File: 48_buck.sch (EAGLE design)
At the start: 31 parts

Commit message: Update with values from quickstart sheet
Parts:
- removed R13: 10K, rcl:R-TRIMM3224W
- added C16: 1uF, rcl:C-EUC1206
- added C17: .1uF, rcl:C-EUC0805
- added C18: .01uF, rcl:C-EUC0805
- added D1, D2: (no value), zetex:VAR2SOT23
- added J1, J2: POWERPOLE_POWER45A_HORIZONTAL_DRILL, powerpoles:POWERPOLE_POWER45A_HORIZONTAL_DRILL
- added J3: POWERPOLE_POWER10AWG, powerpoles:POWERPOLE_POWER10AWG
- added Q1, Q2: BUZ21, transistor-fet:BUZ21
- C1: value 220uF -> 61.2uF; device rcl:CPOL-USE10-25 -> rcl:C-EUC0805
- C10, C11, C12, C13: value 100uF -> 330uF; device rcl:C-EUC0805 -> resistor:CPOL-USE5-10.5
- C14: device rcl:C-EUC0805 -> rcl:C-EUC1210
- C15: value 100uF -> 10uF; device rcl:C-EUC0805 -> rcl:C-EUC1206
- C3: value .22uF -> 910pF
- C4: value 560pF -> 33pF
- C5: value (none) -> 0.1uF
- C6: value (none) -> 1100pF
- C7: value 100uF -> 1uF
- C8: value 1uF -> 0.47uF
- C9: value 100uF -> 1uF; device rcl:C-EUC0805 -> rcl:C-EUC1206
- L1: value 15uH -> 10uH; device rcl:L-US0207/15 -> rcl:L-USTJ5-U2
- R1: value 390K -> 75K; device rcl:R-US_R0805 -> rcl:R-US_R1206
- R10: value 1M -> 10K2
- R11: value 315K -> 1K; device rcl:R-US_R0805 -> rcl:R-TRIMM3224W
- R12: value 10K -> 3m 1%
- R2: value 11K -> 500R; device rcl:R-US_R0805 -> rcl:R-TRIMM3224W
- R3: value 12.4K -> 1K8; device rcl:R-US_R0805 -> rcl:R-US_R1206
- R4: value (none) -> 1M
- R5: value 1K -> 300K
- R6: value 1k -> 12.4K
- R7: value 3m -> 71K5
- R8: value 1M -> 634K
- R9: value 300K -> 1K
- renumbered U$1 to LM5116
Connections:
- removed net N$13: R12.1, R13.S, R5.2
- removed net V+: C1.+, LM5116.VIN, R1.2, R8.2
- new net N$16: R10.1, R11.E, R11.S
- new net N$17: C1.1, D2.C, J2.V+, J3.V+, LM5116.VIN, Q1.D, R1.2, R4.2
- new net N$19: C4.2, LM5116.FB, R10.2, R7.2, R9.1
- new net N$20: C8.2, L1.1, LM5116.SW, Q1.S, Q2.D
- net GND: now also C2.2, C5.2, C6.2, R3.1, R9.2; no longer C3.2, C4.2, LM5116.VCCX, R2.2, R3.2
- net N$1: now also R2.S, R3.2; no longer LM5116.UVLO, R1.1, R2.1
- net N$10: now also C8.1, D1.C, LM5116.HB; no longer C8.2, L1.1, LM5116.SW
- net N$11: now also C2.1, D2.A, LM5116.UVLO, R1.1, R2.A; no longer C10.1, C11.1, C12.1, C13.1, C14.1, C15.1, C7.1, C9.1, L1.2, LM5116.VOUT, R13.A, R5.1
- net N$12: now also LM5116.HO, Q1.G; no longer C8.1, LM5116.HB
- net N$14: now also C10.+, C11.+, C12.+, C13.+, C14.1, C15.1, C16.1, C17.1, C18.1, C7.1, J1.V+, L1.2, LM5116.VCCX, LM5116.VOUT, R11.A; no longer JP1.2, LM5116.EN, R10.2
- net N$15: now also Q2.S, R12.1; no longer R7.1
- net N$2: now also LM5116.EN, R4.1, R5.2; no longer R8.1, R9.2
- net N$3: now also C5.1; no longer C3.1
- net N$4: now also C9.1, D1.A, R8.2; no longer C2.1, R11.2
- net N$5: now also C3.2, R7.1; no longer C5.2, R4.1
- net N$6: now also R6.1; no longer R3.1
- net N$7: now also C3.1, C4.1; no longer C5.1, C6.1
- net N$8: now also LM5116.LO, Q2.G; no longer C6.2, LM5116.FB, R12.2, R4.2, R6.1
- net N$9: now also C6.1, R8.1; no longer C4.1, R11.1
- net PE: now also C1.2, C10.-, C11.-, C12.-, C13.-, C16.2, C17.2, C18.2, J1.GND, J2.GND, J3.GND, JP1.2, R12.2, R5.1; no longer C1.-, C10.2, C11.2, C12.2, C13.2, C2.2, R10.1, R7.2, R9.1
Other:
- note added: "LM5116"
- moved on the sheet: C14, C15, C2, C3, C4, C5, C6, C7, C8, C9, JP1, L1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

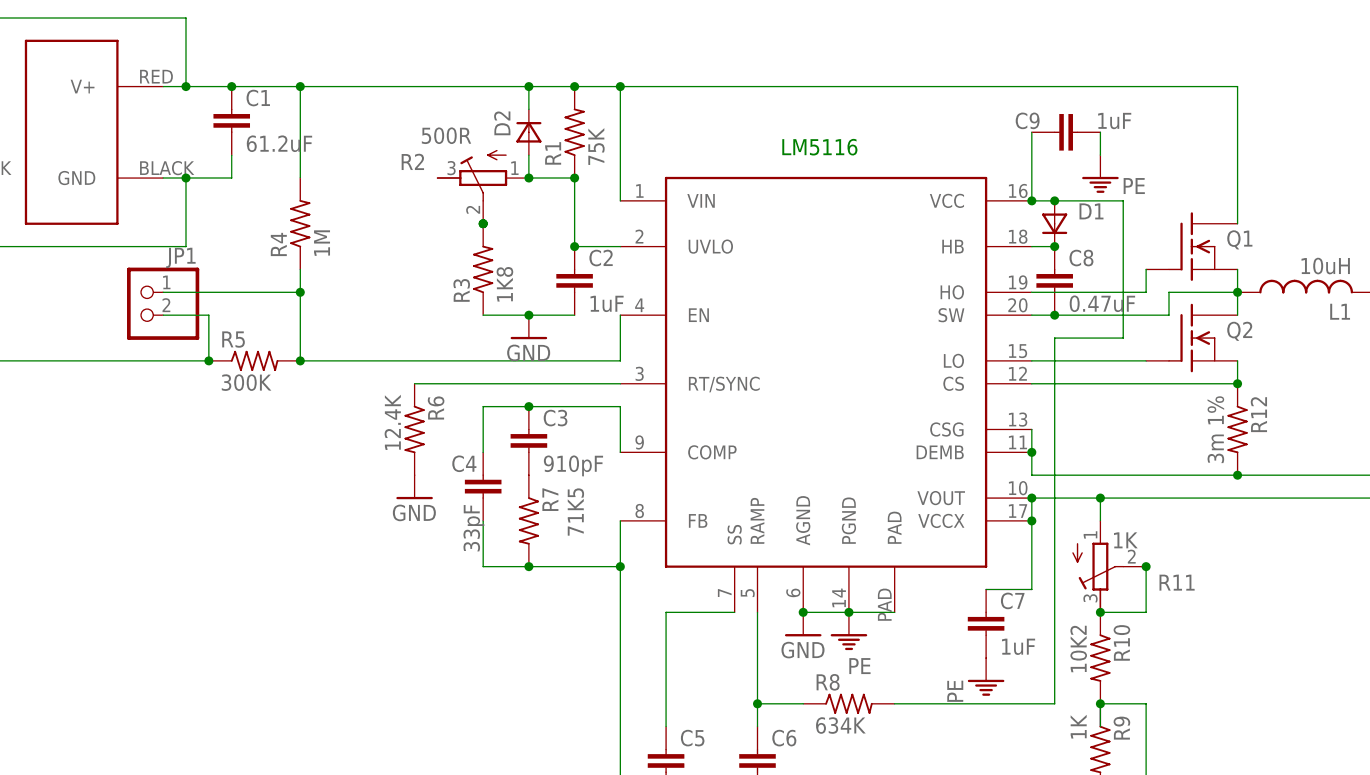
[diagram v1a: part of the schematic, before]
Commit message: Verified schematic, added components to library, started layout
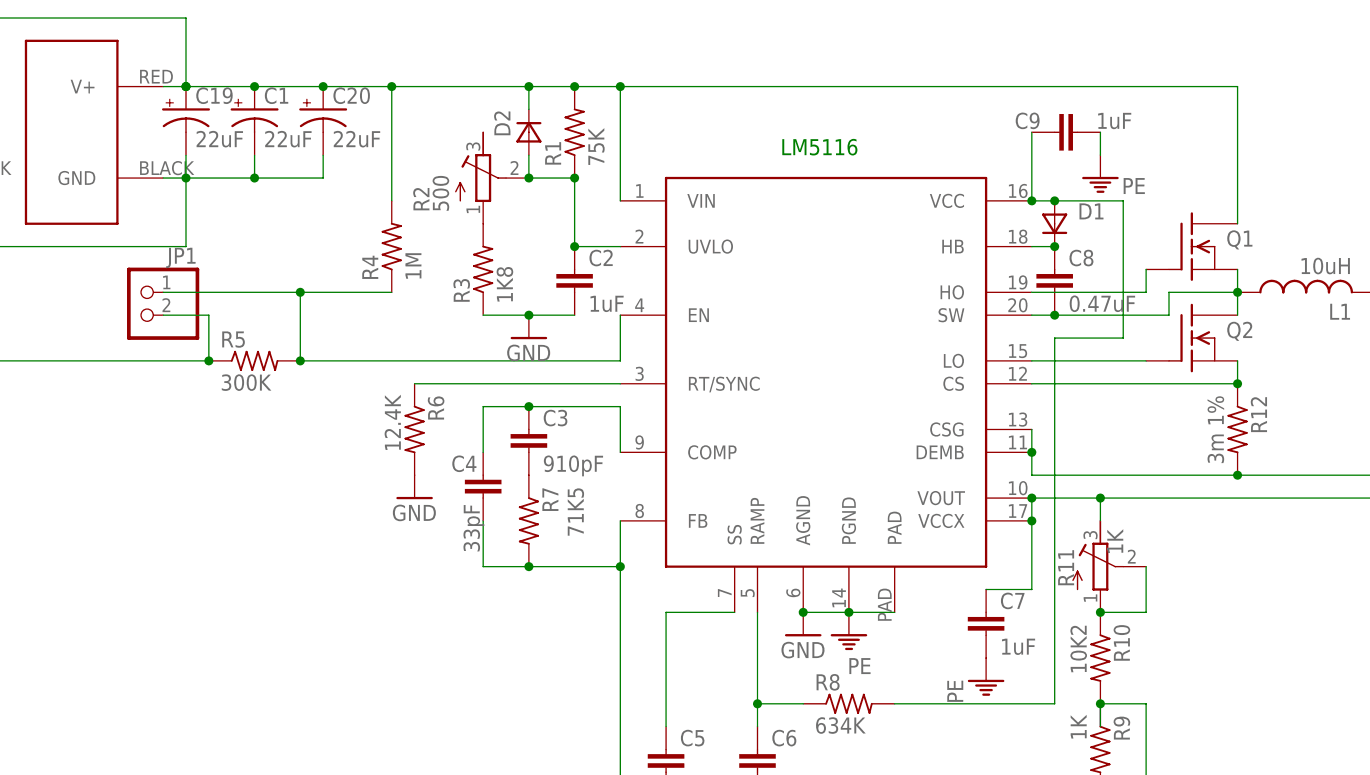
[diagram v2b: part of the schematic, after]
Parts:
- added C19, C20: 22uF, rcl:CPOL-USE3.5-8
- C1: value 61.2uF -> 22uF; device rcl:C-EUC0805 -> rcl:CPOL-USE3.5-8
- C2: device rcl:C-EUC0805 -> rcl:C-EUC1206
- L1: device rcl:L-USTJ5-U2 -> 48buck_library:AIRD-03
- R10: device rcl:R-US_R0805 -> 48buck_library:R2818
- R11: device rcl:R-TRIMM3224W -> 48buck_library:3303X-3
- R2: value 500R -> 500; device rcl:R-TRIMM3224W -> 48buck_library:3303X-3
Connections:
- net N$1: now also R2.A; no longer R2.S
- net N$11: now also R2.S; no longer R2.A
- net N$14: now also R11.E; no longer R11.A
- net N$16: now also R11.A; no longer R11.E
- net N$17: now also C1.+, C19.+, C20.+; no longer C1.1
- net PE: now also C1.-, C19.-, C20.-; no longer C1.2
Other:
- moved on the sheet: R11, R2, R4
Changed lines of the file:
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@@
 <?xml version="1.0" encoding="utf-8"?>
 <!DOCTYPE eagle SYSTEM "eagle.dtd">
-<eagle version="7.2.0">
+<eagle version="7.3.0">
 <drawing>
 <settings>
@@
 <parts>
 <part name="LM5116" library="48buck_library" deviceset="LM5116" device=""/>
-<part name="C1" library="rcl" deviceset="C-EU" device="C0805" value="61.2uF"/>
+<part name="C1" library="rcl" deviceset="CPOL-US" device="E3.5-8" value="22uF"/>
 <part name="PE2" library="supply1" deviceset="PE" device=""/>
 <part name="PE3" library="supply1" deviceset="PE" device=""/>
@@
 <part name="GND4" library="supply1" deviceset="GND" device=""/>
 <part name="GND5" library="supply1" deviceset="GND" device=""/>
-<part name="L1" library="rcl" deviceset="L-US" device="TJ5-U2" value="10uH"/>
+<part name="L1" library="48buck_library" deviceset="AIRD-03" device="" value="10uH"/>
 <part name="JP1" library="pinhead" deviceset="PINHD-1X2" device=""/>
 <part name="R4" library="rcl" deviceset="R-US_" device="R0805" value="1M"/>
@@
 <part name="C12" library="resistor" deviceset="CPOL-US" device="E5-10.5" value="330uF"/>
 <part name="C13" library="resistor" deviceset="CPOL-US" device="E5-10.5" value="330uF"/>
-<part name="R10" library="rcl" deviceset="R-US_" device="R0805" value="10K2"/>
-<part name="R11" library="rcl" deviceset="R-TRIMM" device="3224W" value="1K"/>
-<part name="R2" library="rcl" deviceset="R-TRIMM" device="3224W" value="500R"/>
-<part name="C2" library="rcl" deviceset="C-EU" device="C0805" value="1uF"/>
+<part name="R10" library="48buck_library" deviceset="R2818" device="" value="10K2"/>
+<part name="C2" library="rcl" deviceset="C-EU" device="C1206" value="1uF"/>
 <part name="J1" library="powerpoles" deviceset="POWERPOLE_POWER" device="45A_HORIZONTAL_DRILL"/>
 <part name="J2" library="powerpoles" deviceset="POWERPOLE_POWER" device="45A_HORIZONTAL_DRILL"/>
@@
 <part name="D1" library="zetex" deviceset="VAR2SOT23" device=""/>
 <part name="D2" library="zetex" deviceset="VAR2SOT23" device=""/>
+<part name="C19" library="rcl" deviceset="CPOL-US" device="E3.5-8" value="22uF"/>
+<part name="C20" library="rcl" deviceset="CPOL-US" device="E3.5-8" value="22uF"/>
+<part name="R11" library="48buck_library" deviceset="3303X-3" device="" value="1K"/>
+<part name="R2" library="48buck_library" deviceset="3303X-3" device="" value="500"/>
 </parts>
 <sheets>
@@
 <instances>
 <instance part="LM5116" gate="G$1" x="0" y="0"/>
-<instance part="C1" gate="G$1" x="-43.18" y="15.24"/>
+<instance part="C1" gate="G$1" x="-40.64" y="15.24"/>
 <instance part="PE2" gate="M" x="25.4" y="-43.18" smashed="yes">
 <attribute name="VALUE" x="27.94" y="-45.72" size="1.778" layer="96" rot="R180"/>
@@
 <instance part="L1" gate="G$1" x="76.2" y="-5.08" rot="R90"/>
 <instance part="JP1" gate="G$1" x="-53.34" y="-7.62" rot="MR0"/>
-<instance part="R4" gate="G$1" x="-35.56" y="2.54" rot="R90"/>
+<instance part="R4" gate="G$1" x="-25.4" y="0" rot="R90"/>
 <instance part="R5" gate="G$1" x="-40.64" y="-12.7"/>
 <instance part="PE7" gate="M" x="-71.12" y="-15.24"/>
@@
 <instance part="C12" gate="G$1" x="109.22" y="-7.62"/>
 <instance part="C13" gate="G$1" x="119.38" y="-7.62"/>
-<instance part="R10" gate="G$1" x="53.34" y="-45.72" rot="R270"/>
-<instance part="R11" gate="G$1" x="53.34" y="-35.56" smashed="yes" rot="MR180">
-<attribute name="NAME" x="59.69" y="-36.449" size="1.778" layer="95" rot="MR180"/>
-<attribute name="VALUE" x="54.61" y="-31.75" size="1.778" layer="96" rot="MR180"/>
-</instance>
-<instance part="R2" gate="G$1" x="-15.24" y="7.62" smashed="yes" rot="MR270">
-<attribute name="NAME" x="-21.59" y="8.509" size="1.778" layer="95" rot="MR0"/>
-<attribute name="VALUE" x="-16.51" y="11.43" size="1.778" layer="96" rot="MR0"/>
-</instance>
+<instance part="R10" gate="R$1" x="53.34" y="-45.72" rot="R270"/>
 <instance part="C2" gate="G$1" x="-5.08" y="-2.54"/>
 <instance part="J1" gate="G$1" x="193.04" y="-10.16"/>
@@
 <attribute name="NAME" x="-12.2174" y="15.24" size="1.778" layer="95" rot="MR270"/>
 </instance>
+<instance part="C19" gate="G$1" x="-48.26" y="15.24"/>
+<instance part="C20" gate="G$1" x="-33.02" y="15.24"/>
+<instance part="R11" gate="G$1" x="53.34" y="-35.56" smashed="yes">
+<attribute name="NAME" x="50.419" y="-37.846" size="1.778" layer="95" rot="R90"/>
+<attribute name="VALUE" x="55.88" y="-34.29" size="1.778" layer="96" rot="R90"/>
+</instance>
+<instance part="R2" gate="G$1" x="-15.24" y="7.62"/>
 </instances>
 <busses>
@@
 <wire x1="-71.12" y1="0" x2="-48.26" y2="0" width="0.1524" layer="91"/>
 <wire x1="-48.26" y1="0" x2="-48.26" y2="7.62" width="0.1524" layer="91"/>
-<pinref part="C1" gate="G$1" pin="2"/>
-<wire x1="-43.18" y1="10.16" x2="-43.18" y2="7.62" width="0.1524" layer="91"/>
-<wire x1="-43.18" y1="7.62" x2="-48.26" y2="7.62" width="0.1524" layer="91"/>
+<pinref part="C1" gate="G$1" pin="-"/>
+<wire x1="-40.64" y1="10.16" x2="-40.64" y2="7.62" width="0.1524" layer="91"/>
+<wire x1="-40.64" y1="7.62" x2="-48.26" y2="7.62" width="0.1524" layer="91"/>
 <junction x="-48.26" y="7.62"/>
 <wire x1="-71.12" y1="-12.7" x2="-71.12" y2="0" width="0.1524" layer="91"/>
@@
 <wire x1="-45.72" y1="-7.62" x2="-45.72" y2="-12.7" width="0.1524" layer="91"/>
 <junction x="-45.72" y="-12.7"/>
+<pinref part="C19" gate="G$1" pin="-"/>
+<wire x1="-48.26" y1="10.16" x2="-48.26" y2="7.62" width="0.1524" layer="91"/>
+<pinref part="C20" gate="G$1" pin="-"/>
+<wire x1="-33.02" y1="10.16" x2="-33.02" y2="7.62" width="0.1524" layer="91"/>
+<wire x1="-33.02" y1="7.62" x2="-40.64" y2="7.62" width="0.1524" layer="91"/>
+<junction x="-40.64" y="7.62"/>
 </segment>
 <segment>
@@
 <junction x="-35.56" y="-12.7"/>
 <pinref part="R4" gate="G$1" pin="1"/>
-<wire x1="-35.56" y1="-2.54" x2="-35.56" y2="-5.08" width="0.1524" layer="91"/>
+<wire x1="-25.4" y1="-5.08" x2="-35.56" y2="-5.08" width="0.1524" layer="91"/>
 <pinref part="JP1" gate="G$1" pin="1"/>
 <wire x1="-35.56" y1="-5.08" x2="-35.56" y2="-12.7" width="0.1524" layer="91"/>
 <wire x1="-50.8" y1="-5.08" x2="-35.56" y2="-5.08" width="0.1524" layer="91"/>
 <junction x="-35.56" y="-5.08"/>
-</segment>
-</net>
-<net name="N$1" class="0">
-<segment>
-<pinref part="R2" gate="G$1" pin="S"/>
-<pinref part="R2" gate="G$1" pin="S"/>
-<pinref part="R3" gate="G$1" pin="2"/>
-<junction x="-15.24" y="2.54"/>
-<junction x="-15.24" y="2.54"/>
 </segment>
 </net>
@@
 <pinref part="LM5116" gate="G$1" pin="UVLO"/>
 <wire x1="-5.08" y1="0" x2="0" y2="0" width="0.1524" layer="91"/>
-<pinref part="R2" gate="G$1" pin="A"/>
 <wire x1="-10.16" y1="7.62" x2="-5.08" y2="7.62" width="0.1524" layer="91"/>
 <junction x="-5.08" y="7.62"/>
 <pinref part="D2" gate="A" pin="A"/>
 <wire x1="-10.16" y1="10.16" x2="-10.16" y2="7.62" width="0.1524" layer="91"/>
+<pinref part="R2" gate="G$1" pin="S"/>
 <junction x="-10.16" y="7.62"/>
 </segment>
@@
 <wire x1="-48.26" y1="25.4" x2="-48.26" y2="17.78" width="0.1524" layer="91"/>
 <junction x="-48.26" y="17.78"/>
-<pinref part="C1" gate="G$1" pin="1"/>
-<wire x1="-43.18" y1="17.78" x2="-48.26" y2="17.78" width="0.1524" layer="91"/>
-<junction x="-43.18" y="17.78"/>
-<wire x1="-43.18" y1="17.78" x2="-35.56" y2="17.78" width="0.1524" layer="91"/>
+<pinref part="C1" gate="G$1" pin="+"/>
+<wire x1="-40.64" y1="17.78" x2="-48.26" y2="17.78" width="0.1524" layer="91"/>
+<junction x="-40.64" y="17.78"/>
+<wire x1="-40.64" y1="17.78" x2="-33.02" y2="17.78" width="0.1524" layer="91"/>
 <pinref part="R4" gate="G$1" pin="2"/>
-<wire x1="-35.56" y1="7.62" x2="-35.56" y2="17.78" width="0.1524" layer="91"/>
+<wire x1="-33.02" y1="17.78" x2="-25.4" y2="17.78" width="0.1524" layer="91"/>
+<wire x1="-25.4" y1="5.08" x2="-25.4" y2="17.78" width="0.1524" layer="91"/>
 <wire x1="-5.08" y1="17.78" x2="-10.16" y2="17.78" width="0.1524" layer="91"/>
 <junction x="-5.08" y="17.78"/>
-<junction x="-35.56" y="17.78"/>
+<junction x="-25.4" y="17.78"/>
 <pinref part="D2" gate="A" pin="C"/>
-<wire x1="-10.16" y1="17.78" x2="-35.56" y2="17.78" width="0.1524" layer="91"/>
+<wire x1="-10.16" y1="17.78" x2="-25.4" y2="17.78" width="0.1524" layer="91"/>
 <wire x1="-10.16" y1="15.24" x2="-10.16" y2="17.78" width="0.1524" layer="91"/>
 <junction x="-10.16" y="17.78"/>
+<pinref part="C19" gate="G$1" pin="+"/>
+<junction x="-48.26" y="17.78"/>
+<pinref part="C20" gate="G$1" pin="+"/>
+<junction x="-33.02" y="17.78"/>
 </segment>
 </net>
@@
 <segment>
 <pinref part="R9" gate="G$1" pin="1"/>
-<pinref part="R10" gate="G$1" pin="2"/>
+<pinref part="R10" gate="R$1" pin="2"/>
 <junction x="53.34" y="-50.8"/>
 <wire x1="53.34" y1="-53.34" x2="53.34" y2="-50.8" width="0.1524" layer="91"/>
@@
 <net name="N$14" class="0">
 <segment>
-<pinref part="R11" gate="G$1" pin="A"/>
 <wire x1="53.34" y1="-30.48" x2="53.34" y2="-27.94" width="0.1524" layer="91"/>
 <pinref part="LM5116" gate="G$1" pin="VOUT"/>
@@
 <wire x1="45.72" y1="-38.1" x2="40.64" y2="-38.1" width="0.1524" layer="91"/>
 <junction x="53.34" y="-27.94"/>
+<pinref part="R11" gate="G$1" pin="E"/>
 </segment>
 </net>
 <net name="N$16" class="0">
 <segment>
-<pinref part="R10" gate="G$1" pin="1"/>
-<pinref part="R11" gate="G$1" pin="E"/>
+<pinref part="R10" gate="R$1" pin="1"/>
 <wire x1="53.34" y1="-40.64" x2="58.42" y2="-40.64" width="0.1524" layer="91"/>
+<wire x1="58.42" y1="-40.64" x2="58.42" y2="-35.56" width="0.1524" layer="91"/>
+<pinref part="R11" gate="G$1" pin="A"/>
 <junction x="53.34" y="-40.64"/>
 <pinref part="R11" gate="G$1" pin="S"/>
-<pinref part="R11" gate="G$1" pin="S"/>
-<wire x1="58.42" y1="-40.64" x2="58.42" y2="-35.56" width="0.1524" layer="91"/>
-<junction x="58.42" y="-35.56"/>
-</segment>
-</net>
+</segment>
+</net>
+<net name="N$1" class="0">
+<segment>
+<pinref part="R3" gate="G$1" pin="2"/>
+<pinref part="R2" gate="G$1" pin="A"/>
+</segment>
+</net>
